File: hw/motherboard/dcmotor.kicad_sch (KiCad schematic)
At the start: 2 parts

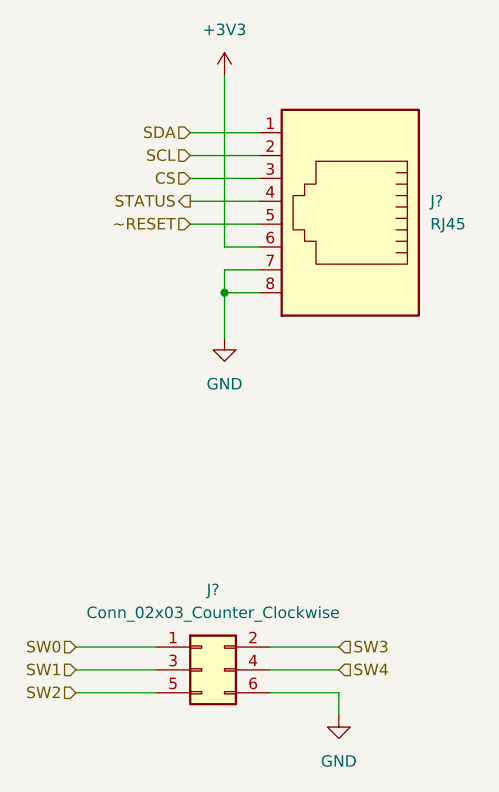
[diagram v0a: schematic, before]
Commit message: Added LEDs and annotation.
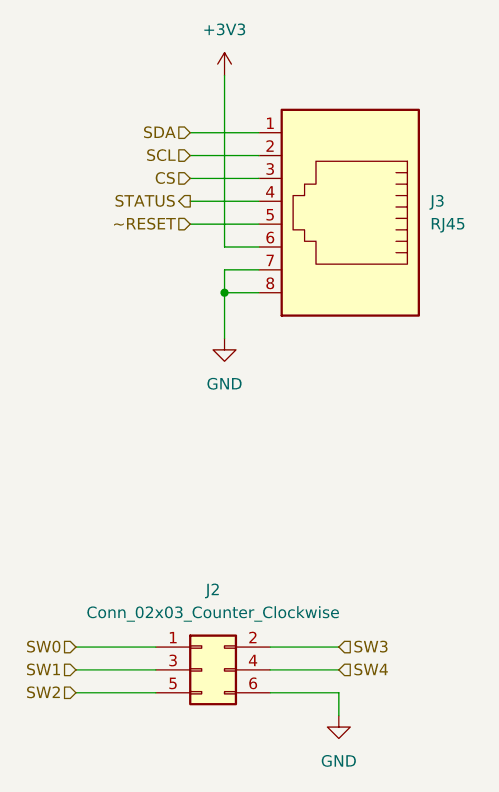
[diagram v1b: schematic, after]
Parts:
- gave numbers to parts that had none: 2
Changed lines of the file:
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@@
   (symbol (lib_id "power:+3V3") (at 182.88 59.69 0) (unit 1)
     (in_bom yes) (on_board yes) (fields_autoplaced)
-    (property "Reference" "#PWR?" (id 0) (at 182.88 63.5 0)
+    (property "Reference" "#PWR05" (id 0) (at 182.88 63.5 0)
       (effects (font (size 1.27 1.27)) hide)
     )
@@
   (symbol (lib_id "Connector:RJ45") (at 196.85 73.66 180) (unit 1)
     (in_bom yes) (on_board yes) (fields_autoplaced)
-    (property "Reference" "J?" (id 0) (at 205.74 73.6599 0)
+    (property "Reference" "J3" (id 0) (at 205.74 73.6599 0)
       (effects (font (size 1.27 1.27)) (justify right))
     )
@@
   (symbol (lib_id "Connector_Generic:Conn_02x03_Odd_Even") (at 180.34 125.73 0) (unit 1)
     (in_bom yes) (on_board yes) (fields_autoplaced)
-    (property "Reference" "J?" (id 0) (at 181.61 116.84 0))
+    (property "Reference" "J2" (id 0) (at 181.61 116.84 0))
     (property "Value" "Conn_02x03_Counter_Clockwise" (id 1) (at 181.61 119.38 0))
     (property "Footprint" "" (id 2) (at 180.34 125.73 0)
@@
   (symbol (lib_id "power:GND") (at 182.88 88.9 0) (unit 1)
     (in_bom yes) (on_board yes) (fields_autoplaced)
-    (property "Reference" "#PWR?" (id 0) (at 182.88 95.25 0)
+    (property "Reference" "#PWR06" (id 0) (at 182.88 95.25 0)
       (effects (font (size 1.27 1.27)) hide)
     )
@@
   (symbol (lib_id "power:GND") (at 195.58 130.81 0) (unit 1)
     (in_bom yes) (on_board yes) (fields_autoplaced)
-    (property "Reference" "#PWR?" (id 0) (at 195.58 137.16 0)
+    (property "Reference" "#PWR07" (id 0) (at 195.58 137.16 0)
       (effects (font (size 1.27 1.27)) hide)
     )
